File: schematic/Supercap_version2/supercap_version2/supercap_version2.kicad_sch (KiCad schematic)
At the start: 22 parts, among them J1 Load, J2 Contactor, J3 FCU, J4 Conn_01x06_Pin, J5 Power, J6 SAFE MODE, Q1 AO3400A, SW1 SW_DIP_x01, U1 STM32F070F6Px

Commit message: new board vatiant begun + asm WFI added in main cycle
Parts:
- removed C3: 1000u, symbol Device:C
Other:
- moved on the sheet: C11, D1, J1, J2, J3, J4, J5, J6, Q1, R12, R13, R14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

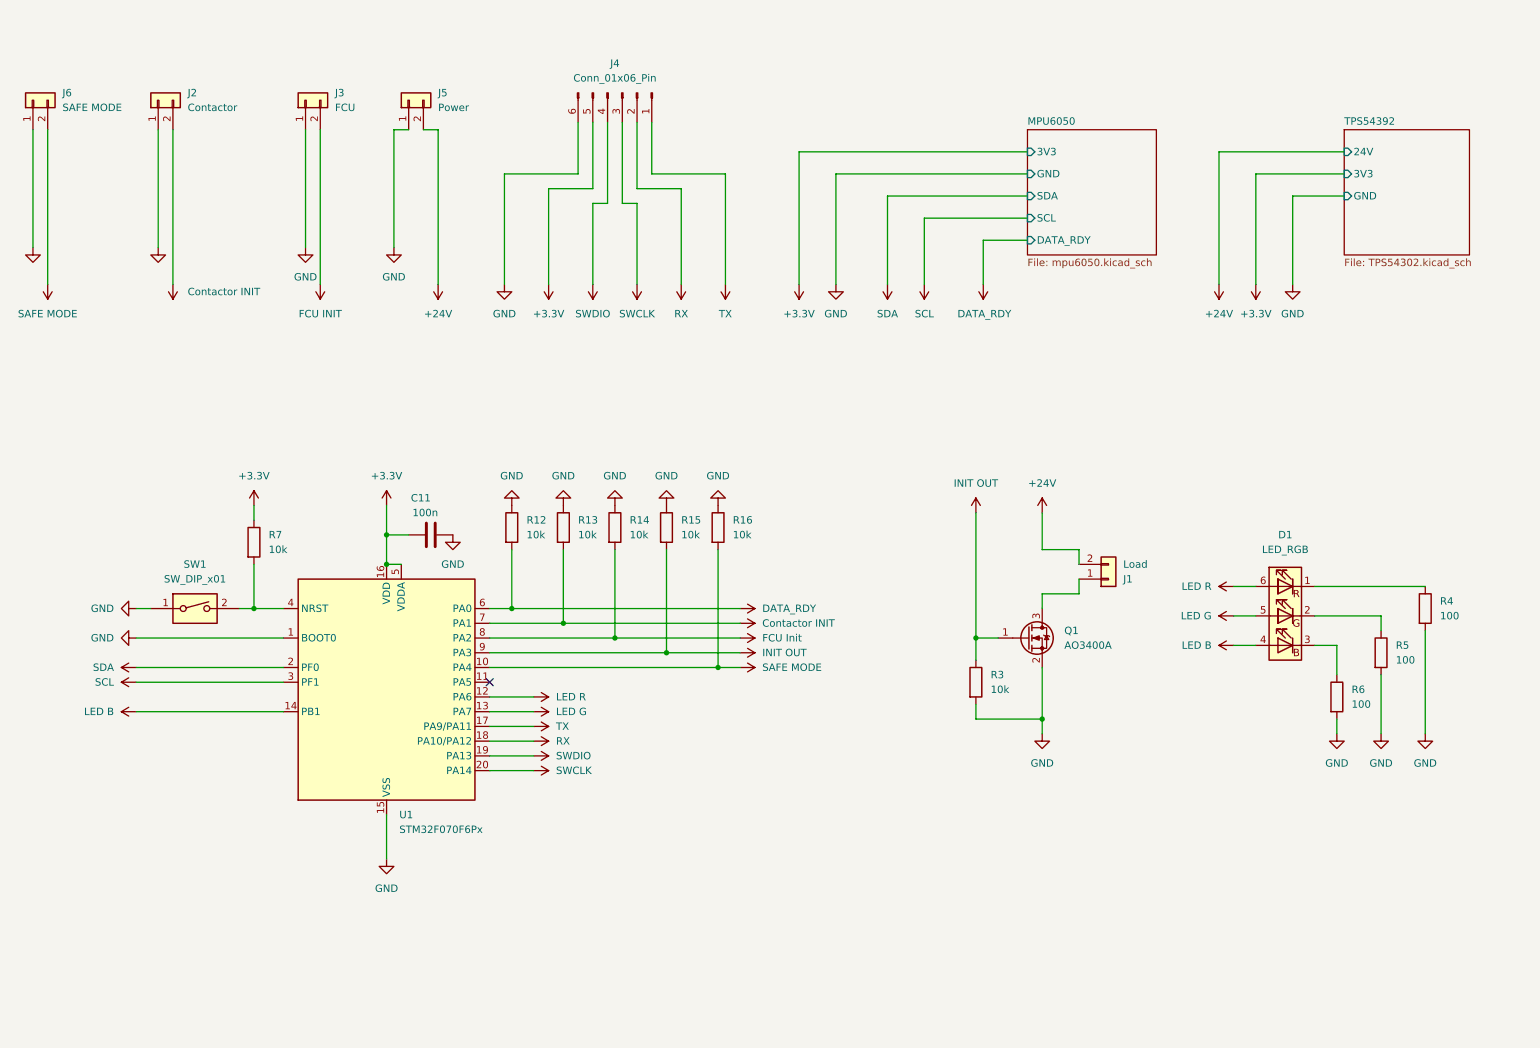
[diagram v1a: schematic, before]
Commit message: TODO: PA5 - hard safe mode check Added hard safe mode via blocking soft safe mode, reed switch added
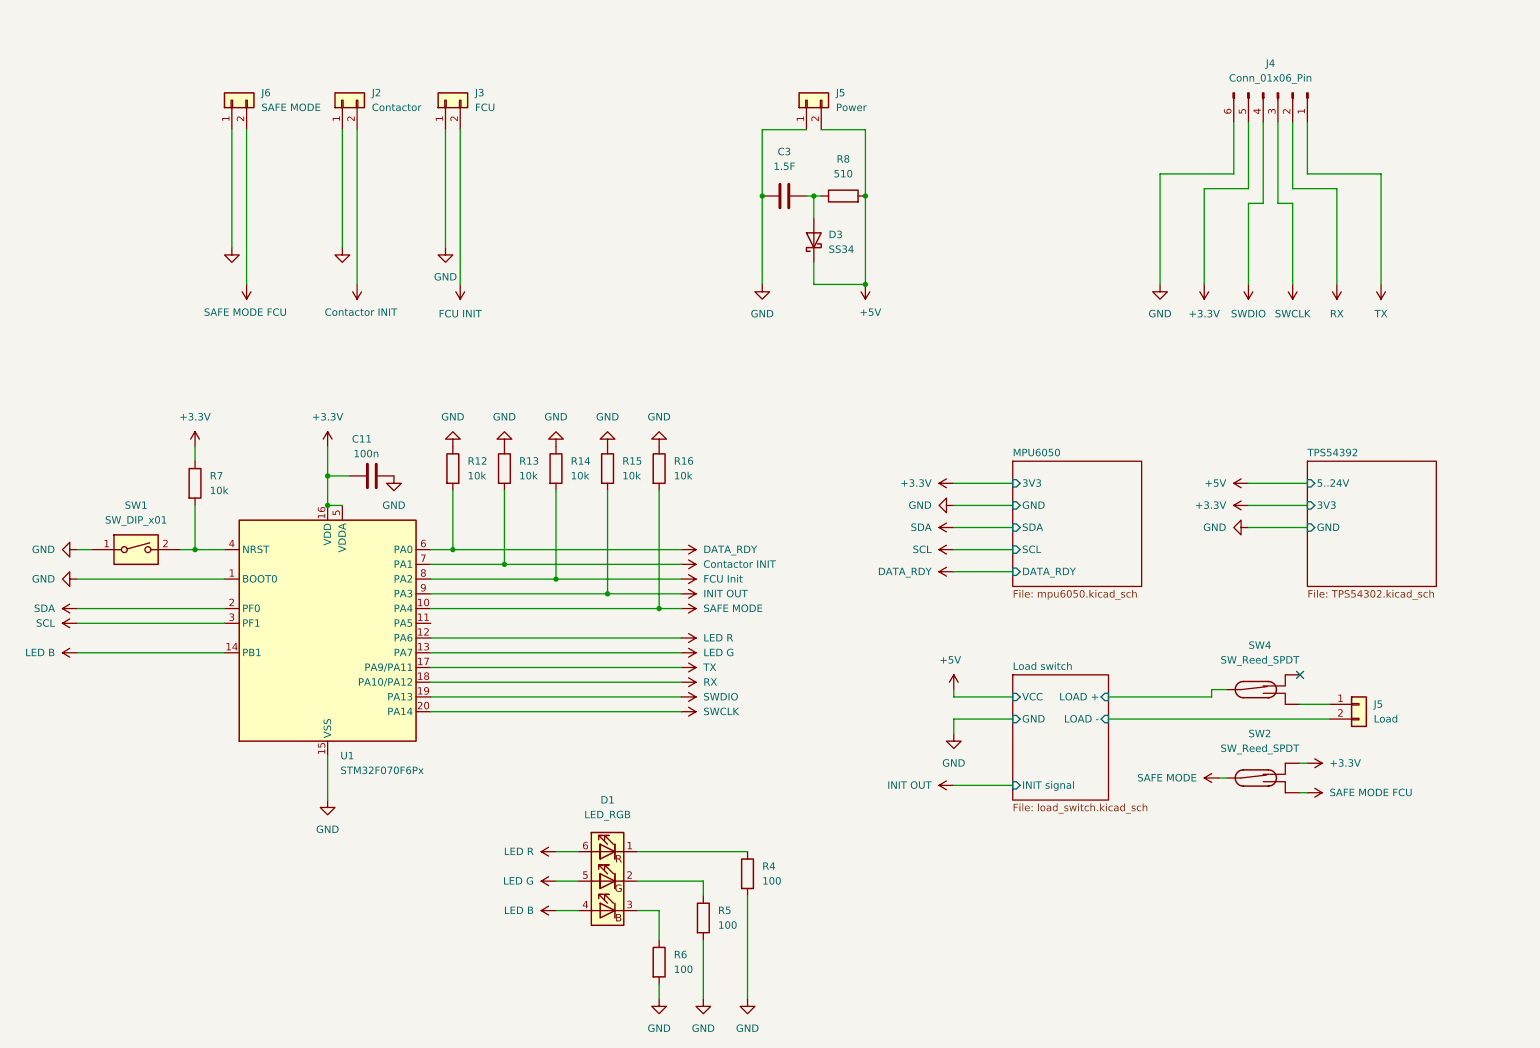
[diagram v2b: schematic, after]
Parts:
- removed J1: Load, Connector_Wire:SolderWire-0.25sqmm_1x02_P4.5mm_D0.65mm_OD2mm, symbol Connector_Generic:Conn_01x02
- removed Q1: AO3400A, Package_TO_SOT_SMD:SOT-23, symbol Transistor_FET:AO3400A
- removed R3: 10k, Resistor_SMD:R_0805_2012Metric_Pad1.20x1.40mm_HandSolder, symbol Device:R
- added C3: 1.5F, symbol Device:C
- added D3: SS34, symbol Device:D_Schottky
- added J5: Load, Connector_Wire:SolderWire-0.25sqmm_1x02_P4.5mm_D0.65mm_OD2mm, symbol Connector_Generic:Conn_01x02
- added R8: 510, symbol Device:R
- added SW2, SW4: SW_Reed_SPDT, symbol Switch:SW_Reed_SPDT
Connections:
- net +3.3V: now also SW2.1
- net GND: now also C3.1
- net SAFE MODE: now also SW2.2; no longer J6.2 (Pin_2)
- net +24V renamed +5V
- net +5V: now also D3.1 (K), R8.2
- new net: J5.1 (Pin_1), SW4.3
- new net: C3.2, D3.2 (A), R8.1
- new net Load switch/LOAD +: SW4.2
- new net Load switch/LOAD -: J5.2 (Pin_2)
- new net SAFE MODE FCU: J6.2 (Pin_2), SW2.3
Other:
- added sheet Load switch (load_switch.kicad_sch)
- sheet TPS54392 ports: added 5..24V; removed 24V
- moved on the sheet: C11, D1, J2, J3, J4, J5, J6, R12, R13, R14, R15, R16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

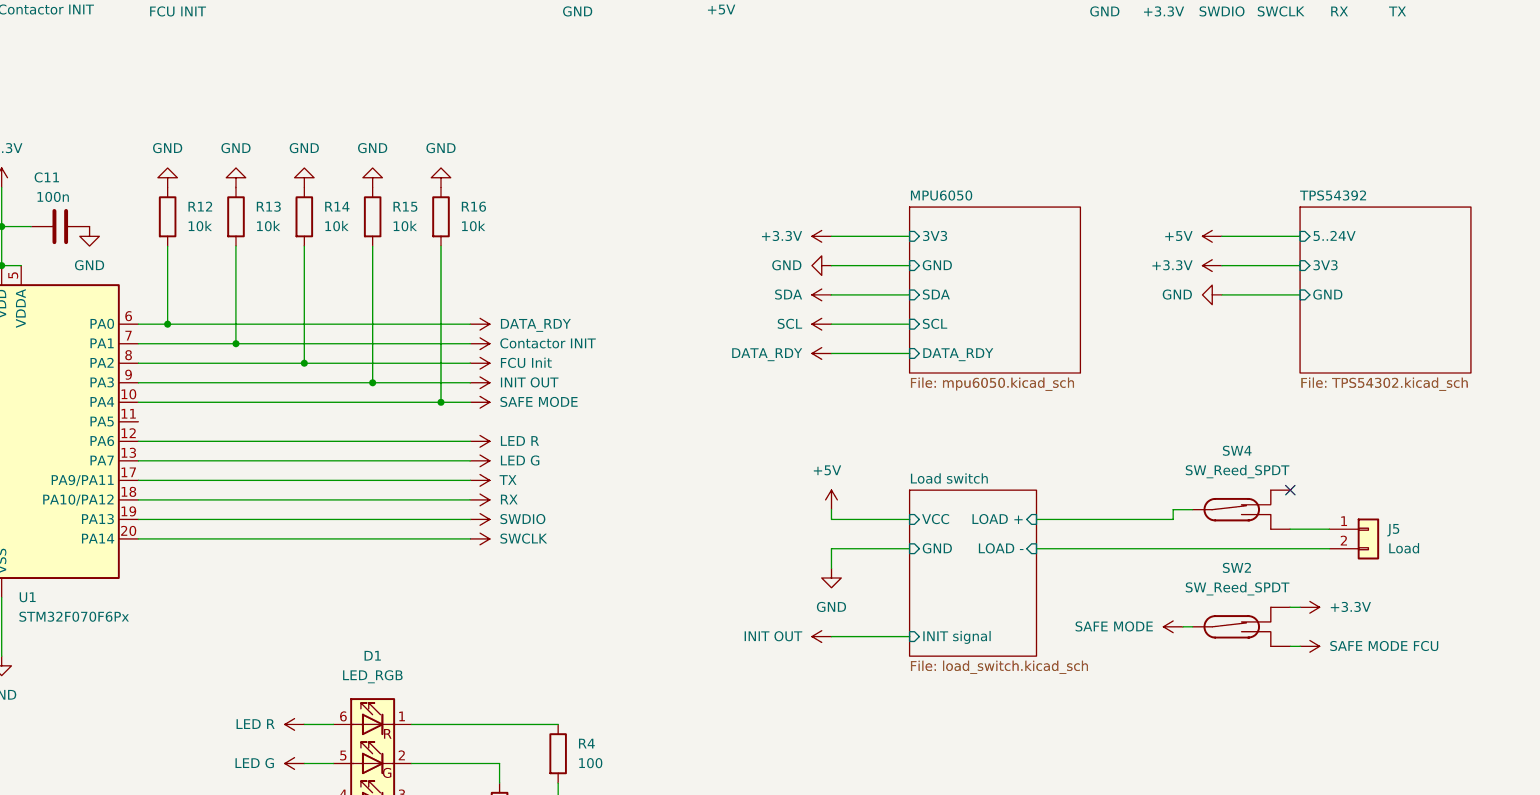
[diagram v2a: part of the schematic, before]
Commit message: Updated board + PA5 hard safe mode (unchecked)
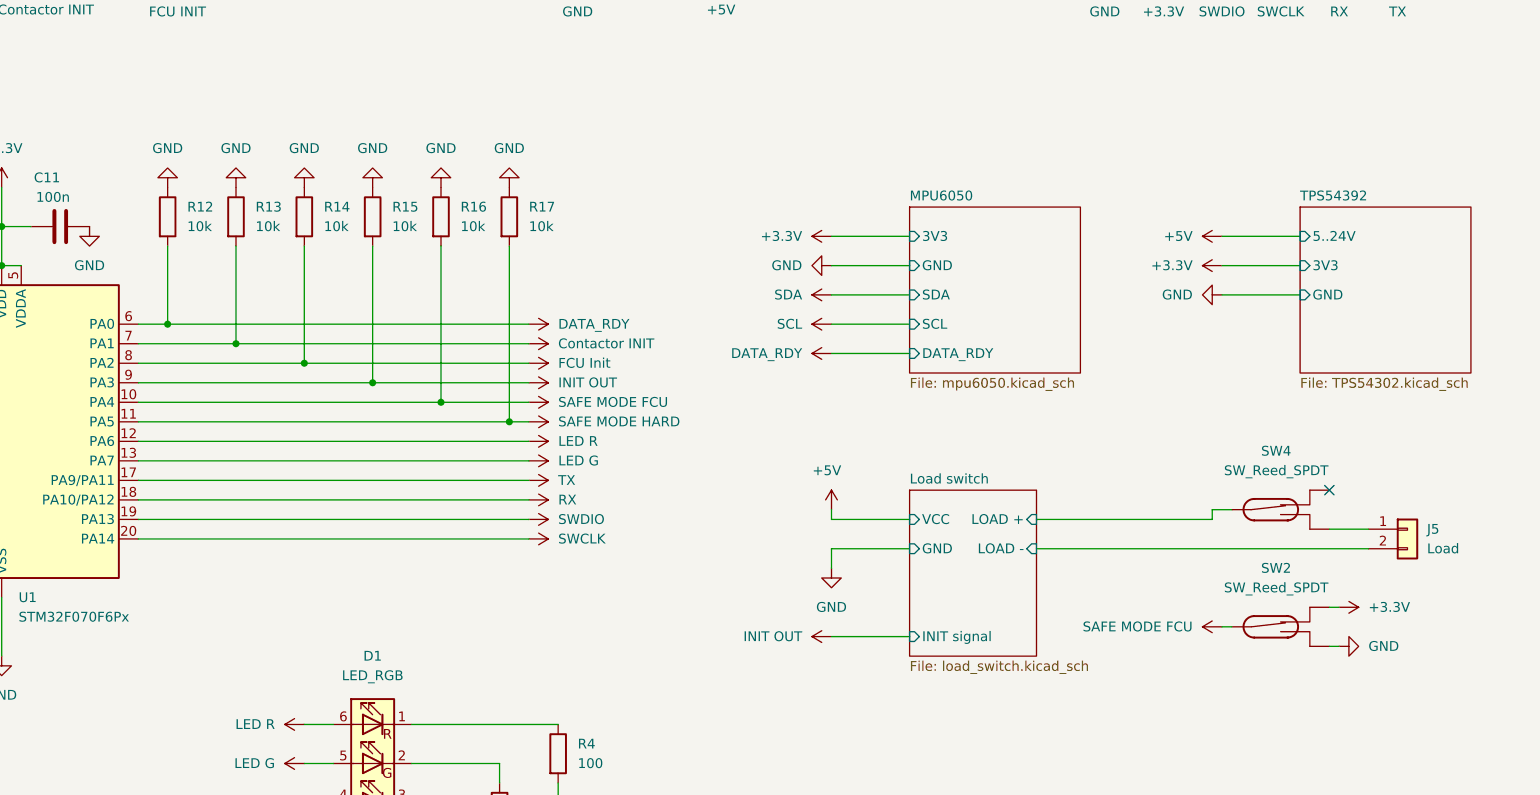
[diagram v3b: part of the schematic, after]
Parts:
- added R17: 10k, Resistor_SMD:R_0805_2012Metric_Pad1.20x1.40mm_HandSolder, symbol Device:R
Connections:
- net SAFE MODE is gone; now on net SAFE MODE FCU: R16.2, SW2.2, U1.10 (PA4)
- net GND: now also SW2.3, R17.1
- net SAFE MODE FCU: no longer SW2.3
- net SAFE MODE HARD: now reaches U1.11 (PA5)
- net SAFE MODE HARD: now also R17.2
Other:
- moved on the sheet: J5, SW2, SW4
